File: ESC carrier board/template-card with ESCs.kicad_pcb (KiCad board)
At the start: 2 copper layers, 111.8 x 83 mm, 18 parts, among them J3 Conn_01x04_Pin, J4 Conn_01x04_Pin, J5 Conn_01x04_Pin, U2 ESC, U4 ESC, U6 ESC

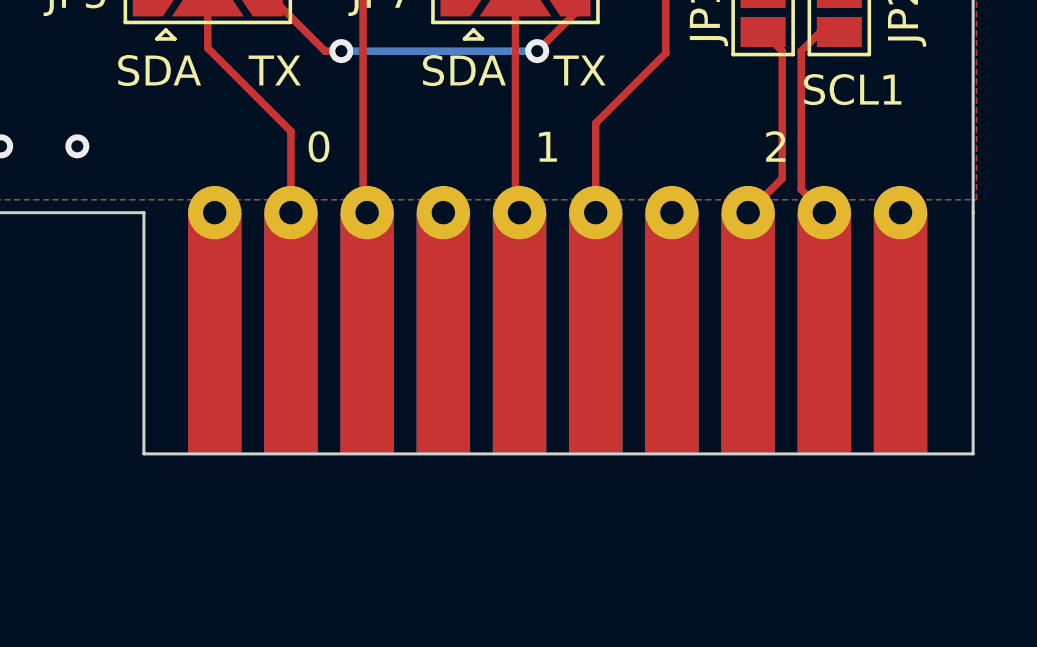
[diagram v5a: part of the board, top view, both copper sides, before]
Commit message: changed the card edge connector as per the new specs
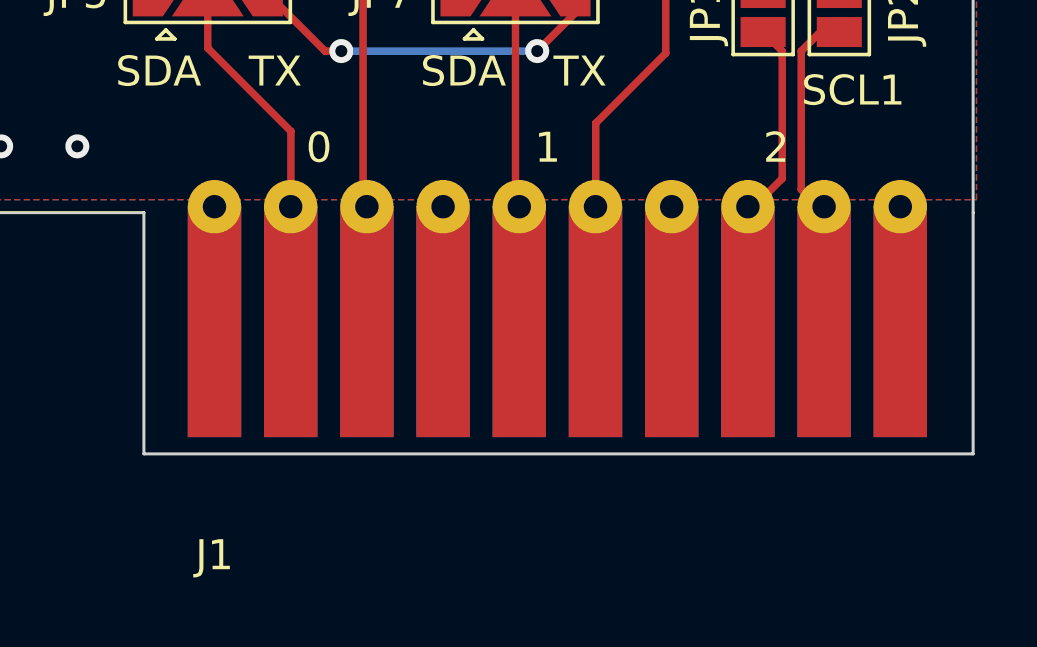
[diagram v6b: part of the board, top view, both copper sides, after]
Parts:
- moved J1 0.20 mm to (172.2, 103.8)
